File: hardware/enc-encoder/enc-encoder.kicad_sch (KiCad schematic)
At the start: 44 parts, among them J1 USB_C_Receptacle, J2 SM03B-SRSS-TB, J3 OQ0232510000G, J4 OQ0232510000G, U6 SP3485CN

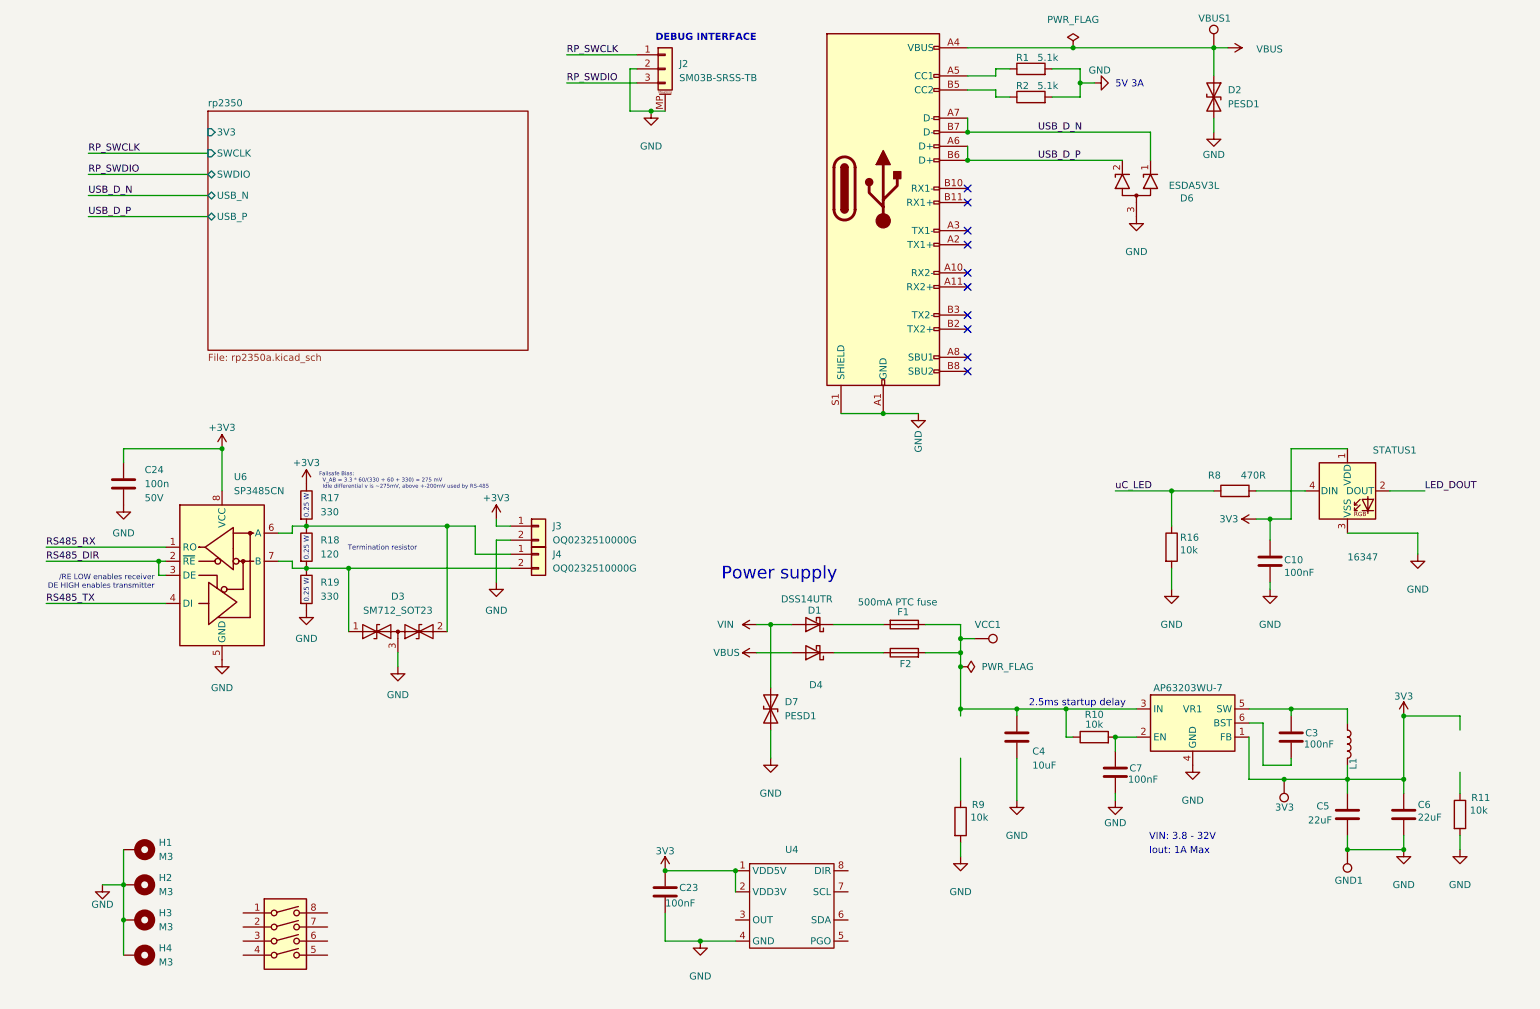
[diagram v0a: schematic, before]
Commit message: Needs checking and ERC fix
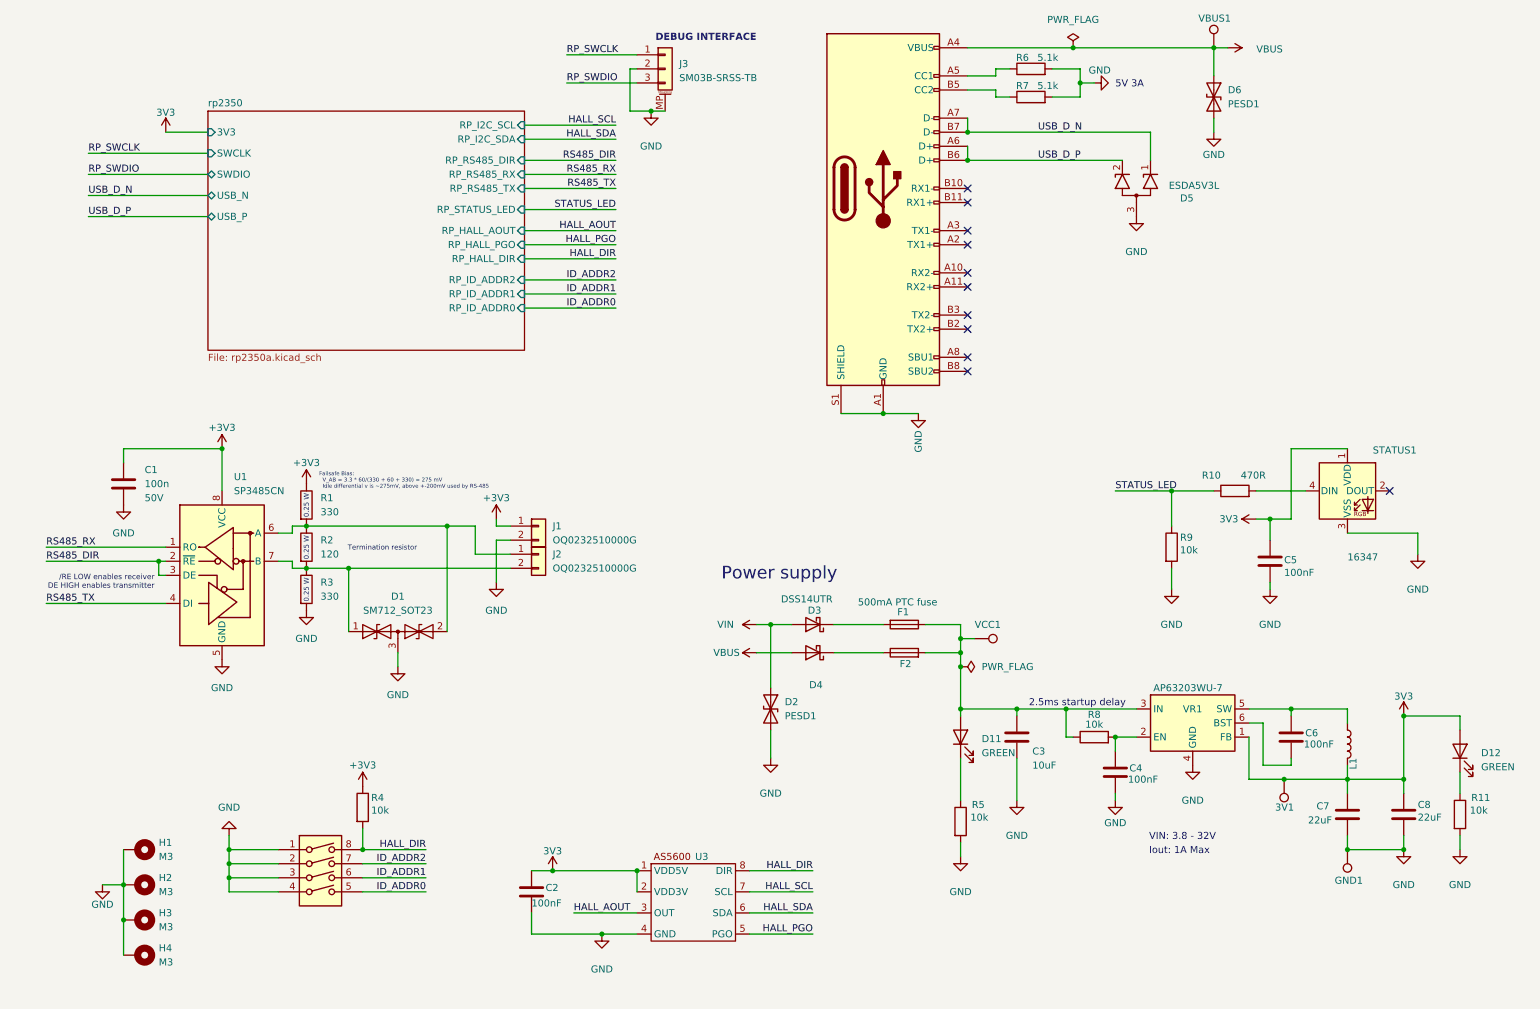
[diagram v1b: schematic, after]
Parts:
- added D11, D12: GREEN, LED_SMD:LED_0805_2012Metric_Pad1.15x1.40mm_HandSolder, symbol Device:LED
- added R4: 10k, Resistor_SMD:R_0603_1608Metric, symbol Device:R
- renumbered 3V3 to 3V1, C24 to C1, C23 to C2, C4 to C3, C7 to C4, C10 to C5, C3 to C6, C5 to C7, C6 to C8, D3 to D1, D7 to D2, D1 to D3, D6 to D5, D2 to D6, J3 to J1, J4 to J2, J2 to J3, J1 to J4, R17 to R1, R8 to R10, R18 to R2, R19 to R3, R9 to R5, R1 to R6, R2 to R7, R10 to R8, R16 to R9, U6 to U1, U5 to U2, U4 to U3
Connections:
- net +3V3: now also R4.1
- net 3V3: now also D12.2 (A)
- net GND: now also U2.1, U2.2, U2.3, U2.4
- net at R11.1: now also D12.1 (K)
- net at C3.1, F1.1, F2.2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: now also D11.2 (A)
- net HALL_AOUT: now reaches U3.3 (OUT)
- net HALL_PGO: now reaches U3.5 (PGO)
- net HALL_SDA: now reaches U3.6 (SDA)
- net HALL_SCL: now reaches U3.7 (SCL)
- net HALL_DIR: now reaches U3.8 (DIR)
- net HALL_DIR: now also U2.8, R4.2
- net at R5.1: now also D11.1 (K)
- net ID_ADDR0: now reaches U2.5
- net ID_ADDR1: now reaches U2.6
- net ID_ADDR2: now reaches U2.7
- net LED_DOUT: no longer names the net of STATUS1.2 (DOUT)
- net uC_LED renamed STATUS_LED
- no-connect marks 10 -> 11
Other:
- sheet rp2350 ports: added RP_HALL_AOUT, RP_HALL_DIR, RP_HALL_PGO, RP_I2C_SCL, RP_I2C_SDA, RP_ID_ADDR0, RP_ID_ADDR1, RP_ID_ADDR2, RP_RS485_DIR, RP_RS485_RX, RP_RS485_TX, RP_STATUS_LED; removed none
- moved on the sheet: C2

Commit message: Feat: Fixed schematic errors, updated BOM
Fixed various schematic errors and missing footprints, models, symbols etc.
Also updated BOM to include active, available, appropriate components
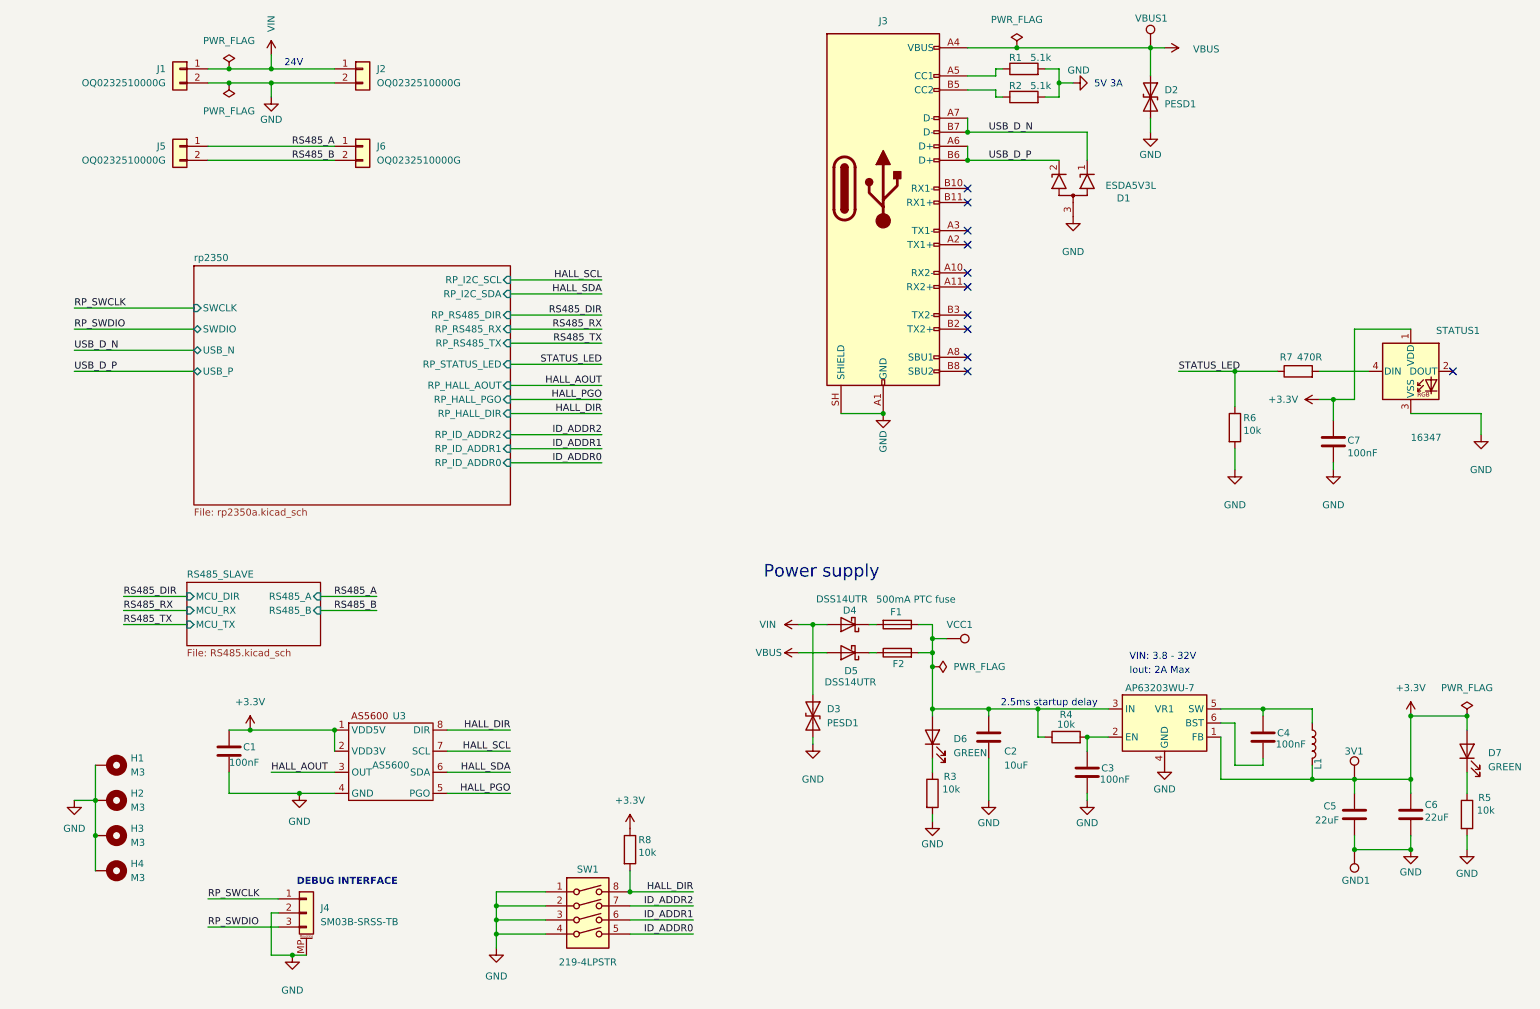
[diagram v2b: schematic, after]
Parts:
- removed C1: 100n, Capacitor_SMD:C_0603_1608Metric, symbol Capacitor:C_100n_50V_0603
- removed D1: SM712_SOT23, Package_TO_SOT_SMD:SOT-23, symbol Diode:SM712_SOT23
- removed D4: DSS14UTR, Diode_SMD:D_SOD-123F, symbol Device:D_Schottky
- removed R1, R3: 330, Resistor_SMD:R_0603_1608Metric, symbol Device:R
- removed R2: 120, Resistor_SMD:R_0603_1608Metric, symbol Device:R
- removed U1: SP3485CN, Package_SO:SOIC-8_3.9x4.9mm_P1.27mm, symbol Interface_UART:SP3485CN
- removed U2: (no value), footprints:SW_218-4LPSTR, symbol component_library:4_DIP
- added D5: DSS14UTR, Diode_SMD:D_SOD-123F, symbol Device:D_Schottky
- added J5, J6: OQ0232510000G, ConnectorsOther:AnyTek_OQ_3.81mm_90_2P_TriangleKeyLock, symbol Connector_Generic:Conn_01x02
- added SW1: 219-4LPSTR, SMD:SW_218-4LPSTR, symbol component_library:4_DIP
- C1: renamed from C2; footprint Capacitor_SMD:C_0603_1608Metric -> Capacitor_SMD:C_0402_1005Metric_Pad0.74x0.62mm_HandSolder; Supplier (none) -> DigiKey; Supplier Link (none) -> https://www.digikey.com.au/en/products/detail/murata-electr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; Supplier Part No (none) -> 490-10698-1-ND; distributors part number 1276-1012-2-ND -> (none); manufactuer part number CL10F104ZB8NNNC -> (none); manufacturer Samsung Electro-Mechanics -> (none)
- C2: renamed from C3; footprint Capacitor_SMD:C_0603_1608Metric -> Capacitor_SMD:C_0805_2012Metric_Pad1.18x1.45mm_HandSolder; Supplier (none) -> DigiKey; Supplier Link (none) -> https://www.digikey.com.au/en/products/detail/murata-electr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; Supplier Part No (none) -> 490-3886-1-ND; distributors part number 1276-1192-2-ND -> (none); manufactuer part number CL10A106KP8NNNC -> (none); manufacturer Samsung Electro-Mechanics -> (none)
- C3: renamed from C4; footprint Capacitor_SMD:C_0603_1608Metric -> Capacitor_SMD:C_0402_1005Metric_Pad0.74x0.62mm_HandSolder; Supplier (none) -> DigiKey; Supplier Link (none) -> https://www.digikey.com.au/en/products/detail/murata-electr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; Supplier Part No (none) -> 490-10698-1-ND; distributors part number 1276-1012-2-ND -> (none); manufactuer part number CL10F104ZB8NNNC -> (none); manufacturer Samsung Electro-Mechanics -> (none)
- C4: renamed from C6; footprint Capacitor_SMD:C_0603_1608Metric -> Capacitor_SMD:C_0402_1005Metric_Pad0.74x0.62mm_HandSolder; Supplier (none) -> DigiKey; Supplier Link (none) -> https://www.digikey.com.au/en/products/detail/murata-electr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; Supplier Part No (none) -> 490-10698-1-ND; distributors part number 1276-1012-2-ND -> (none); manufactuer part number CL10F104ZB8NNNC -> (none); manufacturer Samsung Electro-Mechanics -> (none)
- C5: renamed from C7; footprint Capacitor_SMD:C_0603_1608Metric -> Capacitor_SMD:C_0603_1608Metric_Pad1.08x0.95mm_HandSolder; Supplier (none) -> DigiKey; Supplier Link (none) -> https://www.digikey.com.au/en/products/detail/murata-electr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; Supplier Part No (none) -> 490-13243-1-ND; distributors part number 1276-1274-2-ND -> (none); manufactuer part number CL10A226MP8NUNE -> (none); manufacturer Samsung Electro-Mechanics -> (none)
- C6: renamed from C8; footprint Capacitor_SMD:C_0603_1608Metric -> Capacitor_SMD:C_0603_1608Metric_Pad1.08x0.95mm_HandSolder; Supplier (none) -> DigiKey; Supplier Link (none) -> https://www.digikey.com.au/en/products/detail/murata-electr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; Supplier Part No (none) -> 490-13243-1-ND; distributors part number 1276-1274-2-ND -> (none); manufactuer part number CL10A226MP8NUNE -> (none); manufacturer Samsung Electro-Mechanics -> (none)
- C7: renamed from C5; footprint Capacitor_SMD:C_0603_1608Metric -> Capacitor_SMD:C_0402_1005Metric_Pad0.74x0.62mm_HandSolder; Supplier (none) -> DigiKey; Supplier Link (none) -> https://www.digikey.com.au/en/products/detail/murata-electr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; Supplier Part No (none) -> 490-10698-1-ND; distributors part number 1276-1012-2-ND -> (none); manufactuer part number CL10F104ZB8NNNC -> (none); manufacturer Samsung Electro-Mechanics -> (none)
- D1: renamed from D5; footprint Package_TO_SOT_SMD:SOT-416 -> Package_TO_SOT_SMD:SOT-23_Handsoldering; Supplier (none) -> DigiKey; Supplier Link (none) -> https://www.digikey.com.au/en/products/detail/stmicroelectr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; Supplier Part No (none) -> 497-6632-1-ND; distributors part number 497-6632-2-ND -> (none); manufactuer part number ESDA5V3L -> (none); manufacturer STMicroelectronics -> (none)
- D2: renamed from D6; Supplier (none) -> DigiKey; Supplier Link (none) -> https://www.digikey.com.au/en/products/detail/nexperia-usa-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; Supplier Part No (none) -> 1727-PESD1CANFD33L-QYLCT-ND; distributors part number 1727-PESD1CANFD33L-QYLTR-ND -> (none); manufactuer part number PESD1CANFD33L-QYL -> (none); manufacturer Nexperia USA Inc. -> (none)
- D3: renamed from D2; Supplier (none) -> DigiKey; Supplier Link (none) -> https://www.digikey.com.au/en/products/detail/nexperia-usa-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; Supplier Part No (none) -> 1727-PESD1CANFD33L-QYLCT-ND; distributors part number 1727-PESD1CANFD33L-QYLTR-ND -> (none); manufactuer part number PESD1CANFD33L-QYL -> (none); manufacturer Nexperia USA Inc. -> (none)
- D4: renamed from D3; Supplier (none) -> DigiKey; Supplier Link (none) -> https://www.digikey.com.au/en/products/detail/smc-diode-sol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; Supplier Part No (none) -> 1655-DSS14UCT-ND; distributors part number 1655-DSS14UTR-ND -> (none); manufactuer part number DSS14U -> (none); manufacturer SMC Diode Solutions -> (none)
- D6: renamed from D11; Digikey Part Number 350-5991180147FTR-ND -> (none); Supplier (none) -> DigiKey; Supplier Link (none) -> https://www.digikey.com.au/en/products/detail/dialight/5991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; Supplier Part No (none) -> 350-5991180147FCT-ND
- D7: renamed from D12; Digikey Part Number 350-5991180147FTR-ND -> (none); Supplier (none) -> DigiKey; Supplier Link (none) -> https://www.digikey.com.au/en/products/detail/dialight/5991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; Supplier Part No (none) -> 350-5991180147FCT-ND
- F1: Supplier (none) -> DigiKey; Supplier Link (none) -> https://www.digikey.com.au/en/products/detail/yageo/SMD1812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; Supplier Part No (none) -> 13-SMD1812B050TF/30CT-ND; distributors part number 13-SMD1812B050TF/30TR-ND -> (none); manufactuer part number SMD1812B050TF/30 -> (none); manufacturer YAGEO -> (none)
- F2: footprint Fuse:Fuse_0603_1608Metric -> Fuse:Fuse_0603_1608Metric_Pad1.05x0.95mm_HandSolder; Supplier (none) -> DigiKey; Supplier Link (none) -> https://www.digikey.com.au/en/products/detail/bourns-inc/SF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; Supplier Part No (none) -> SF-0603S050-2CT-ND; distributors part number SF-0603S050-2TR-ND -> (none); manufactuer part number SF-0603S050-2 -> (none); manufacturer Bourns Inc. -> (none)
- J2: Supplier (none) -> DigiKey; Supplier Link (none) -> https://www.digikey.com/en/products/detail/amphenol-anytek/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; Supplier Part No (none) -> 609-3819-ND
- J3: renamed from J4; Supplier (none) -> DigiKey; Supplier Link (none) -> https://www.digikey.com.au/en/products/detail/amphenol-cs-c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; Supplier Part No (none) -> 12401610E4#2ACT-ND; distributors part number 12401610E4#2ATR-ND -> (none); manufactuer part number 12401610E4#2A -> (none); manufacturer Amphenol ICC (Commercial Products) -> (none)
- J4: renamed from J3; Supplier (none) -> DigiKey; Supplier Link (none) -> https://www.digikey.com.au/en/products/detail/jst-sales-ame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; Supplier Part No (none) -> 455-SM03B-SRSS-TBCT-ND
- L1: Supplier (none) -> DigiKey; Supplier Link (none) -> https://www.digikey.com.au/en/products/detail/tai-tech-adva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; Supplier Part No (none) -> 4816-HPC4018NF-4R7MCT-ND; distributors part number 4816-HPC4018NF-4R7MTR-ND -> (none); manufactuer part number HPC 4018NF-4R7M -> (none); manufacturer TAI-TECH Advanced Electronics Co., Ltd. -> (none)
- R1: renamed from R6; footprint (none) -> Resistor_SMD:R_0402_1005Metric_Pad0.72x0.64mm_HandSolder; Supplier (none) -> DigiKey; Supplier Link (none) -> https://www.digikey.com.au/en/products/detail/yageo/RC0402F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; Supplier Part No (none) -> 311-5.10KLRCT-ND
- R2: renamed from R7; footprint (none) -> Resistor_SMD:R_0402_1005Metric_Pad0.72x0.64mm_HandSolder; Supplier (none) -> DigiKey; Supplier Link (none) -> https://www.digikey.com.au/en/products/detail/yageo/RC0402F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; Supplier Part No (none) -> 311-5.10KLRCT-ND
- R3: renamed from R5; footprint Resistor_SMD:R_0603_1608Metric -> Resistor_SMD:R_0603_1608Metric_Pad0.98x0.95mm_HandSolder; Supplier (none) -> DigiKey; Supplier Link (none) -> https://www.digikey.com.au/en/products/detail/yageo/RC0603F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; Supplier Part No (none) -> 311-10.0KHRCT-ND; distributors part number 311-10.0KHRTR-ND -> (none); manufactuer part number RC0603FR-0710KL -> (none); manufacturer YAGEO -> (none)
- R4: renamed from R8; footprint Resistor_SMD:R_0402_1005Metric -> Resistor_SMD:R_0603_1608Metric_Pad0.98x0.95mm_HandSolder; Supplier (none) -> DigiKey; Supplier Link (none) -> https://www.digikey.com.au/en/products/detail/yageo/RC0603F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; Supplier Part No (none) -> 311-10.0KHRCT-ND; distributors part number 1276-3431-2-ND -> (none); manufactuer part number RC1005F103CS -> (none); manufacturer Samsung Electro-Mechanics -> (none)
- R5: renamed from R11; footprint Resistor_SMD:R_0603_1608Metric -> Resistor_SMD:R_0603_1608Metric_Pad0.98x0.95mm_HandSolder; Supplier (none) -> DigiKey; Supplier Link (none) -> https://www.digikey.com.au/en/products/detail/yageo/RC0603F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; Supplier Part No (none) -> 311-10.0KHRCT-ND; distributors part number 311-10.0KHRTR-ND -> (none); manufactuer part number RC0603FR-0710KL -> (none); manufacturer YAGEO -> (none)
- R6: renamed from R9; footprint Resistor_SMD:R_0603_1608Metric -> Resistor_SMD:R_0603_1608Metric_Pad0.98x0.95mm_HandSolder; Supplier (none) -> DigiKey; Supplier Link (none) -> https://www.digikey.com.au/en/products/detail/yageo/RC0603F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; Supplier Part No (none) -> 311-10.0KHRCT-ND; distributors part number 311-10.0KHRTR-ND -> (none); manufactuer part number RC0603FR-0710KL -> (none); manufacturer YAGEO -> (none)
- R7: renamed from R10; footprint Resistor_SMD:R_0603_1608Metric -> Resistor_SMD:R_0603_1608Metric_Pad0.98x0.95mm_HandSolder; Supplier (none) -> DigiKey; Supplier Link (none) -> https://www.digikey.com.au/en/products/detail/yageo/RC0603J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; Supplier Part No (none) -> 311-470GRCT-ND; distributors part number 311-470GRTR-ND -> (none); manufactuer part number RC0603JR-07470RL -> (none); manufacturer YAGEO -> (none)
- R8: renamed from R4; footprint Resistor_SMD:R_0603_1608Metric -> Resistor_SMD:R_0603_1608Metric_Pad0.98x0.95mm_HandSolder; Supplier (none) -> DigiKey; Supplier Link (none) -> https://www.digikey.com.au/en/products/detail/yageo/RC0603F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; Supplier Part No (none) -> 311-10.0KHRCT-ND; distributors part number 311-10.0KHRTR-ND -> (none); manufactuer part number RC0603FR-0710KL -> (none); manufacturer YAGEO -> (none)
- STATUS1: Supplier (none) -> DigiKey; Supplier Link (none) -> https://www.digikey.com.au/en/products/detail/sparkfun-elec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; Supplier Part No (none) -> 1568-16347CT-ND; distributors part number 1568-16347TR-ND -> (none); manufactuer part number 16347 -> (none); manufacturer SparkFun Electronics -> (none)
- U3: value (none) -> AS5600
- VR1: Supplier (none) -> DigiKey; Supplier Link (none) -> https://www.digikey.com.au/en/products/detail/diodes-incorp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; Supplier Part No (none) -> AP63203WU-7DICT-ND; distributors part number AP63203WU-7DITR-ND -> (none); manufactuer part number AP63203WU-7 -> (none); manufacturer Diodes Incorporated -> (none)
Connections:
- net 3V3 is gone; now on net +3.3V: 3V1.1, C1.1, C5.1, C6.1, C7.1, D7.2 (A), L1.2, STATUS1.1 (VDD), U3.1 (VDD5V), U3.2 (VDD3V), VR1.1 (FB)
- net GND: now also J2.2 (Pin_2), J3.SH (SHIELD), SW1.1, SW1.2, SW1.3, SW1.4; no longer J3.S1 (SHIELD)
- net HALL_DIR: now also SW1.8
- net ID_ADDR0: now also SW1.5
- net ID_ADDR1: now also SW1.6
- net ID_ADDR2: now also SW1.7
- net VBUS: now also D5.2 (A)
- net VIN: now also J1.1 (Pin_1), J2.1 (Pin_1)
- net at F2.1: now also D5.1 (K)
- net +3V3 renamed +3.3V
- net +3.3V: no longer J1.1 (Pin_1)
- new net RS485_A: J5.1 (Pin_1), J6.1 (Pin_1)
- new net RS485_B: J5.2 (Pin_2), J6.2 (Pin_2)
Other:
- added sheet RS485_SLAVE (RS485.kicad_sch)
- sheet rp2350 ports: added none; removed 3V3
- note added: "24V"
- note added: "Iout: 2A Max"
- note removed: "/RE LOW enables receiver DE HIGH enables transmitter"
- note removed: "0.25 W"
- note removed: "Failsafe Bias: V_AB = 3.3 * 60/(330 + 60 + 330) = 275 mV Idle differential v is ~275mV, above +-200mV used by RS-485"
- note removed: "Iout: 1A Max"
- note removed: "Termination resistor"
- moved on the sheet: 3V1, C1, C2, C3, C4, C5, C6, C7, D1, D2, D3, D4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

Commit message: Feat: Encoder PCB microcontroller layout
Finished microcontroller layout requirements. Additionally fixed schematic BOM and other footprints.
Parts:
- H1, H2, H3, H4: footprint MountingHole:MountingHole_3.2mm_M3_DIN965_Pad -> MountingHole:MountingHole_2.2mm_M2_DIN965_Pad
- U3: Supplier (none) -> DigiKey; Supplier Link (none) -> https://www.digikey.com.au/en/products/detail/infineon-tech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; Supplier Part No (none) -> 448-AS5600-ASOM-SOIC8CT-ND
- renumbered J5 to J2, J2 to J5
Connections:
- net +3.3V: now also SW1.8, U3.8 (DIR); no longer R8.1
- net GND: now also J5.1 (Pin_1), R8.1; no longer J5.2 (Pin_2), SW1.1
- net RS485_A: now also J2.2 (Pin_2); no longer J2.1 (Pin_1)
- net RS485_B: now also J2.1 (Pin_1); no longer J2.2 (Pin_2)
- net VIN: now also J5.2 (Pin_2); no longer J5.1 (Pin_1)
- removed net HALL_DIR: R8.2, SW1.8, U3.8 (DIR)
- new net: R8.2, SW1.1
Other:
- sheet RS485_SLAVE: file RS485.kicad_sch -> RS485_slave.kicad_sch

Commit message: Feat: Encoder PCB Power layout and routing
Added 3.3V voltage regulator traces and routing to the board
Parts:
- D1: footprint Package_TO_SOT_SMD:SOT-23_Handsoldering -> Package_TO_SOT_SMD:SOT-23-3
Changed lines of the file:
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@@
 			)
 		)
-		(property "Footprint" "Package_TO_SOT_SMD:SOT-23_Handsoldering"
+		(property "Footprint" "Package_TO_SOT_SMD:SOT-23-3"
 			(at 195.58 48.26 0)
 			(hide yes)
